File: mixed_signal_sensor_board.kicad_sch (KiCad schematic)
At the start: 59 parts, among them J1 Conn_01x02, J3 Conn_01x06, Q1 IRLML5103TRPBF, SW1 SW_Push, SW2 SW_Push, U1 TMP117xxDRV, U2 LM27762, U3 MagI3C_171013201, U4 TPS7A20xxxDBV, U5 TPS7A20xxxDBV, U6 ADS131M08xPBS, U7 STM32L552CEUx, Y1 SG-8018CE_8.192M-TJHSA

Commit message: New pyro layout, SWDIO, SWCLK, USART2 TX RX, 70x50mm board
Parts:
- added J23: PYRO_ARM, Connector_JST:JST_PH_S2B-PH-SM4-TB_1x02-1MP_P2.00mm_Horizontal, symbol Connector_Generic:Conn_01x02
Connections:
- net +24V: now also J23.1 (Pin_1)
- new net ARM: J23.2 (Pin_2)
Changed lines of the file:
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@@
 	)
 	(symbol
+		(lib_id "Connector_Generic:Conn_01x02")
+		(at 316.23 185.42 0)
+		(mirror y)
+		(unit 1)
+		(body_style 1)
+		(exclude_from_sim no)
+		(in_bom yes)
+		(on_board yes)
+		(in_pos_files yes)
+		(dnp no)
+		(property "Reference" "J23"
+			(at 311.658 185.42 0)
+			(show_name no)
+			(do_not_autoplace no)
+			(effects
+				(font
+					(size 1.27 1.27)
+				)
+			)
+		)
+		(property "Value" "PYRO_ARM"
+			(at 313.436 187.96 0)
+			(show_name no)
+			(do_not_autoplace no)
+			(effects
+				(font
+					(size 1.27 1.27)
+				)
+				(justify left)
+			)
+		)
+		(property "Footprint" "Connector_JST:JST_PH_S2B-PH-SM4-TB_1x02-1MP_P2.00mm_Horizontal"
+			(at 316.23 185.42 0)
+			(hide yes)
+			(show_name no)
+			(do_not_autoplace no)
+			(effects
+				(font
+					(size 1.27 1.27)
+				)
+			)
+		)
+		(property "Datasheet" ""
+			(at 316.23 185.42 0)
+			(hide yes)
+			(show_name no)
+			(do_not_autoplace no)
+			(effects
+				(font
+					(size 1.27 1.27)
+				)
+			)
+		)
+		(property "Description" "Generic connector, single row, 01x02, script generated (kicad-library-utils/schlib/autogen/connector/)"
+			(at 316.23 185.42 0)
+			(hide yes)
+			(show_name no)
+			(do_not_autoplace no)
+			(effects
+				(font
+					(size 1.27 1.27)
+				)
+			)
+		)
+		(pin "2"
+		)
+		(pin "1"
+		)
+		(instances
+			(project "mixed_signal_sensor_board"
+				(path "/5c142d60-6b5a-463f-88b9-a177eae7f51b"
+					(reference "J23")
+					(unit 1)
+				)
+			)
+		)
+	)
+	(symbol
 		(lib_id "Switch:SW_Push")
 		(at 177.8 214.63 0)
@@
 	)
 	(symbol
+		(lib_id "power:+5V")
+		(at 321.31 187.96 270)
+		(unit 1)
+		(body_style 1)
+		(exclude_from_sim no)
+		(in_bom yes)
+		(on_board yes)
+		(in_pos_files yes)
+		(dnp no)
+		(fields_autoplaced yes)
+		(property "Reference" "#PWR0113"
+			(at 317.5 187.96 0)
+			(hide yes)
+			(show_name no)
+			(do_not_autoplace no)
+			(effects
+				(font
+					(size 1.27 1.27)
+				)
+			)
+		)
+		(property "Value" "ARM"
+			(at 325.12 187.9599 90)
+			(show_name no)
+			(do_not_autoplace no)
+			(effects
+				(font
+					(size 1.27 1.27)
+				)
+				(justify left)
+			)
+		)
+		(property "Footprint" ""
+			(at 321.31 187.96 0)
+			(hide yes)
+			(show_name no)
+			(do_not_autoplace no)
+			(effects
+				(font
+					(size 1.27 1.27)
+				)
+			)
+		)
+		(property "Datasheet" ""
+			(at 321.31 187.96 0)
+			(hide yes)
+			(show_name no)
+			(do_not_autoplace no)
+			(effects
+				(font
+					(size 1.27 1.27)
+				)
+			)
+		)
+		(property "Description" "Power symbol creates a global label with name \"+5V\""
+			(at 321.31 187.96 0)
+			(hide yes)
+			(show_name no)
+			(do_not_autoplace no)
+			(effects
+				(font
+					(size 1.27 1.27)
+				)
+			)
+		)
+		(pin "1"
+		)
+		(instances
+			(project "mixed_signal_sensor_board"
+				(path "/5c142d60-6b5a-463f-88b9-a177eae7f51b"
+					(reference "#PWR0113")
+					(unit 1)
+				)
+			)
+		)
+	)
+	(symbol
 		(lib_id "power:GND")
 		(at 247.65 166.37 270)
@@
 					(unit 1)
 				)
+			)
+		)
+	)
+	(symbol
+		(lib_id "power:+5V")
+		(at 321.31 185.42 270)
+		(unit 1)
+		(body_style 1)
+		(exclude_from_sim no)
+		(in_bom yes)
+		(on_board yes)
+		(in_pos_files yes)
+		(dnp no)
+		(fields_autoplaced yes)
+		(property "Reference" "#PWR0114"
+			(at 317.5 185.42 0)
+			(hide yes)
+			(show_name no)
+			(do_not_autoplace no)
+			(effects
+				(font
+					(size 1.27 1.27)
+				)
+			)
+		)
+		(property "Value" "+24V"
+			(at 325.12 185.4199 90)
+			(show_name no)
+			(do_not_autoplace no)
+			(effects
+				(font
+					(size 1.27 1.27)
+				)
+				(justify left)
+			)
+		)
+		(property "Footprint" ""
+			(at 321.31 185.42 0)
+			(hide yes)
+			(show_name no)
+			(do_not_autoplace no)
+			(effects
+				(font
+					(size 1.27 1.27)
+				)
+			)
+		)
+		(property "Datasheet" ""
+			(at 321.31 185.42 0)
+			(hide yes)
+			(show_name no)
+			(do_not_autoplace no)
+			(effects
+				(font
+					(size 1.27 1.27)
+				)
+			)
+		)
+		(property "Description" "Power symbol creates a global label with name \"+5V\""
+			(at 321.31 185.42 0)
+			(hide yes)
+			(show_name no)
+			(do_not_autoplace no)
+			(effects
+				(font
+					(size 1.27 1.27)
+				)
+			)
+		)
+		(pin "1"
+		)
+		(instances
+			(project "mixed_signal_sensor_board"
+				(path "/5c142d60-6b5a-463f-88b9-a177eae7f51b"
+					(reference "#PWR0114")
+					(unit 1)
+				)

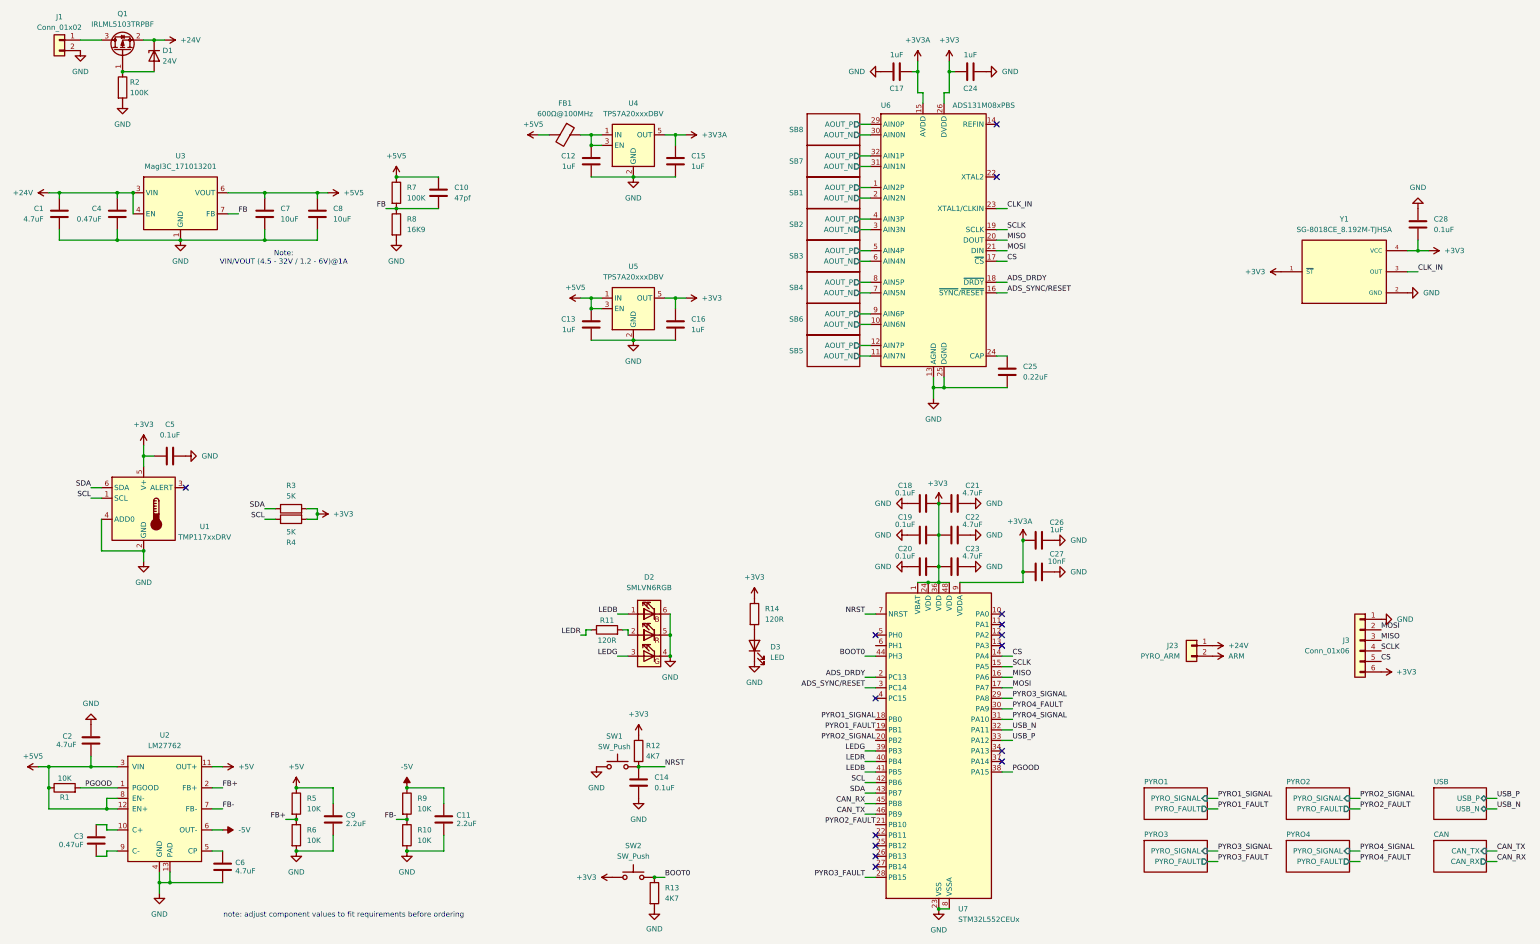
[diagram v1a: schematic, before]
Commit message: PYRO done, schematic structure/convention update, pyro and reverse polarity components selected
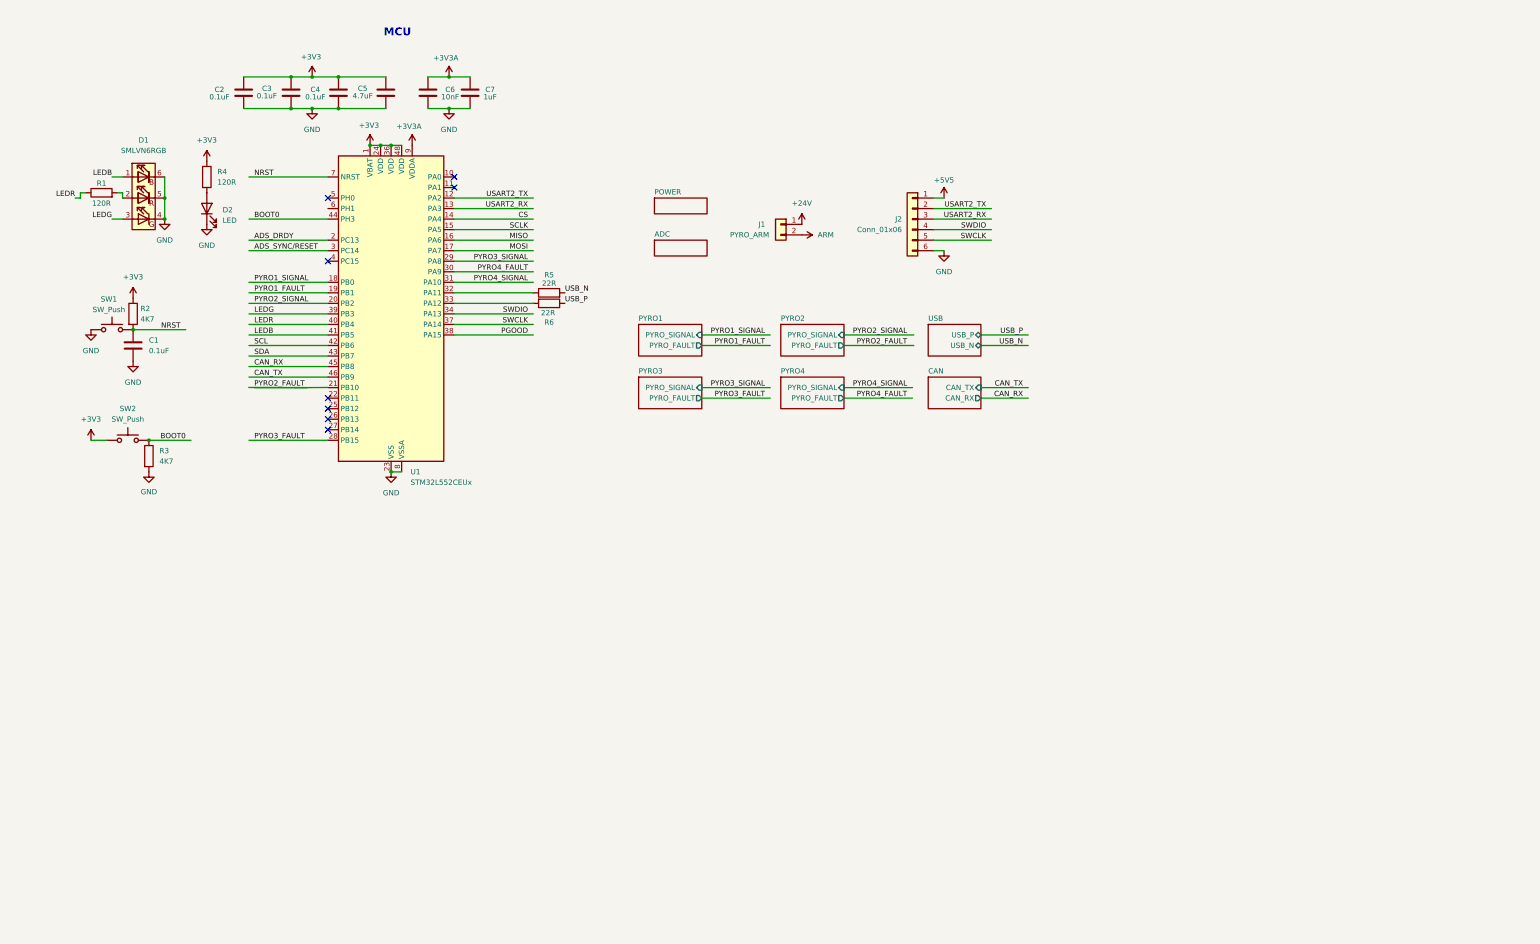
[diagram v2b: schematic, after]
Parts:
- removed C1: 4.7uF, Capacitor_SMD:C_0603_1608Metric, symbol Device:C
- removed C10: 47pf, Capacitor_SMD:C_0402_1005Metric, symbol Device:C
- removed C11, C9: 2.2uF, Capacitor_SMD:C_0402_1005Metric, symbol Device:C
- removed C12, C13, C15, C16, C17, C24: 1uF, Capacitor_SMD:C_0402_1005Metric, symbol Device:C
- removed C18, C19, C20, C28: 0.1uF, Capacitor_SMD:C_0402_1005Metric, symbol Device:C
- removed C21, C22, C23, C6: 4.7uF, Capacitor_SMD:C_0402_1005Metric, symbol Device:C
- removed C25: 0.22uF, Capacitor_SMD:C_0402_1005Metric, symbol Device:C
- removed C7, C8: 10uF, Capacitor_SMD:C_0603_1608Metric, symbol Device:C
- removed D1: 24V, Diode_SMD:D_0402_1005Metric, symbol Device:D_Zener
- removed FB1: 600Ω@100MHz, Inductor_SMD:L_0402_1005Metric, symbol Device:FerriteBead
- removed J1: Conn_01x02, Connector_JST:JST_PH_S2B-PH-SM4-TB_1x02-1MP_P2.00mm_Horizontal, symbol Connector_Generic:Conn_01x02
- removed Q1: IRLML5103TRPBF, Package_TO_SOT_SMD:SOT-23, symbol Transistor_FET:Q_PMOS_GSD
- removed R1, R10, R9: 10K, Resistor_SMD:R_0402_1005Metric, symbol Device:R
- removed R2, R7: 100K, Resistor_SMD:R_0402_1005Metric, symbol Device:R
- removed R3, R4: 5K, Resistor_SMD:R_0402_1005Metric, symbol Device:R
- removed R8: 16K9, Resistor_SMD:R_0402_1005Metric, symbol Device:R
- removed U1: TMP117xxDRV, Package_SON:WSON-6-1EP_2x2mm_P0.65mm_EP1x1.6mm, symbol Sensor_Temperature:TMP117xxDRV
- removed U2: LM27762, Package_SON:WSON-12-1EP_3x2mm_P0.5mm_EP1x2.65_ThermalVias, symbol Regulator_SwitchedCapacitor:LM27762
- removed U3: MagI3C_171013201, MagI3C_171013201:MagI3C_171013201, symbol MagI3C_171013201:MagI3C_171013201
- removed U4, U5: TPS7A20xxxDBV, Package_TO_SOT_SMD:SOT-23-5, symbol Regulator_Linear:TPS7A20xxxDBV
- removed U6: ADS131M08xPBS, Package_QFP:TQFP-32_5x5mm_P0.5mm, symbol Analog_ADC:ADS131M08xPBS
- removed Y1: SG-8018CE_8.192M-TJHSA, SG-8018CE_8.9152M-TJHSA0:OSC_SG-8018CE_8.9152M-TJHSA0, symbol SG-8018CE_8.9152M-TJHSA0:SG-8018CE_8.9152M-TJHSA0
- C2: value 4.7uF -> 0.1uF; LCSC Part (none) -> C71629; Voltage Rating (none) -> 16V
- C3: value 0.47uF -> 0.1uF; LCSC Part (none) -> C71629; Voltage Rating (none) -> 16V
- C4: value 0.47uF -> 0.1uF; footprint Capacitor_SMD:C_0603_1608Metric -> Capacitor_SMD:C_0402_1005Metric; LCSC Part (none) -> C71629; Voltage Rating (none) -> 16V
- C5: value 0.1uF -> 4.7uF; LCSC Part (none) -> C71629; Voltage Rating (none) -> 16V
- R5, R6: value 10K -> 22R; LCSC Part (none) -> C482106
- renumbered C14 to C1, C27 to C6, C26 to C7, D2 to D1, D3 to D2, J23 to J1, J3 to J2, R11 to R1, R12 to R2, R13 to R3, R14 to R4, U7 to U1
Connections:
- net +24V: no longer C4.2
- net +3V3: now also C2.2, C3.2, C4.2; no longer J2.6 (Pin_6)
- net +5V5: now also J2.1 (Pin_1); no longer C2.2
- net CS: no longer J2.5 (Pin_5)
- net GND: now also C3.1, J2.6 (Pin_6); no longer J2.1 (Pin_1), R6.2
- net MISO: no longer J2.3 (Pin_3)
- net MOSI: no longer J2.2 (Pin_2)
- net PYRO2_FAULT: no longer U1.21 (PB10)
- net SCLK: no longer J2.4 (Pin_4)
- net USB_N: now also R5.2; no longer U1.32 (PA11)
- net USB_P: now also R6.1; no longer U1.33 (PA12)
- net USART2_TX: now reaches U1.12 (PA2)
- net USART2_TX: now also J2.2 (Pin_2)
- net USART2_RX: now reaches U1.13 (PA3)
- net USART2_RX: now also J2.3 (Pin_3)
- net SWDIO: now reaches U1.34 (PA13)
- net SWDIO: now also J2.4 (Pin_4)
- net SWCLK: now reaches U1.37 (PA14)
- net SWCLK: now also J2.5 (Pin_5)
- net +5V: no longer names the net of R5.1
- net +5V: now also U1.32 (PA11)
- removed net FB+: R5.2, R6.1
- new net: R6.2, U1.33 (PA12)
- no-connect marks 15 -> 8
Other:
- removed sheet SB1
- removed sheet SB2
- removed sheet SB3
- removed sheet SB4
- removed sheet SB5
- removed sheet SB6
- removed sheet SB7
- removed sheet SB8
- added sheet ADC (adc.kicad_sch)
- added sheet POWER (power.kicad_sch)
- note added: "MCU"
- note removed: "Note: VIN/VOUT (4.5 - 32V / 1.2 - 6V)@1A"
- note removed: "note: adjust component values to fit requirements before ordering"
- moved on the sheet: C1, C6, C7, D1, D2, J1, J2, R1, R2, R3, R4, SW1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
